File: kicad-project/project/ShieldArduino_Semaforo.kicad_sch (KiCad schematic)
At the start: 48 parts, among them IC1 TPS54302DDCR, J1 Conn_01x01, J10 Conn_01x01, J11 Conn_01x01, J12 Conn_01x01, J2 Conn_01x01, J3 Conn_01x01, J4 Conn_01x01, J5 Conn_01x01, J6 Conn_01x01, J7 Conn_01x01, J8 Conn_01x01, J9 Conn_01x01, P1 Power, P2 Analog, P3 Digital, P4 Digital, P5 CONN_01X01, P6 CONN_01X01, P7 CONN_01X01, P8 CONN_01X01, Q1 PMOS, U2 LM321, U4 MCP2542FD-E/MF

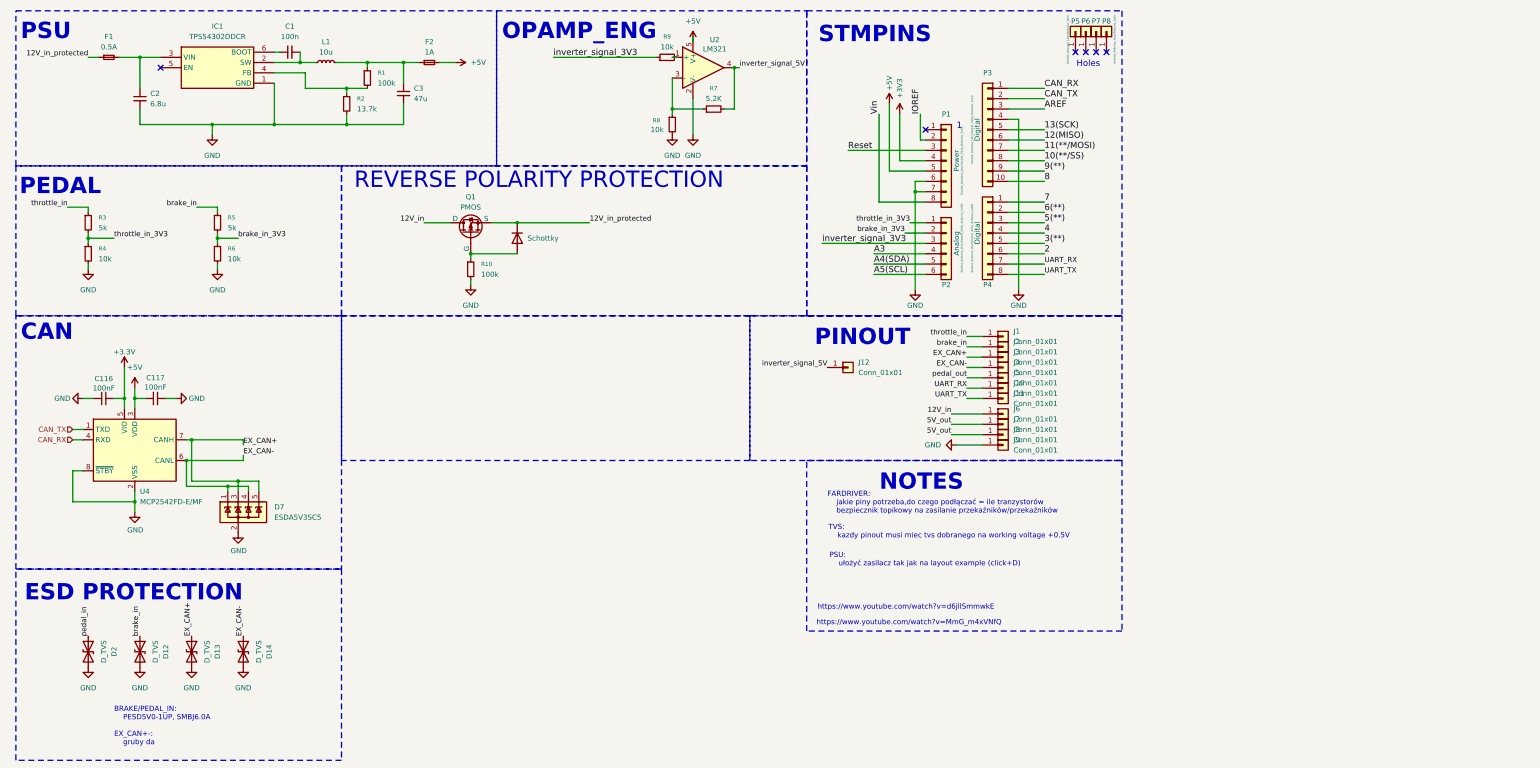
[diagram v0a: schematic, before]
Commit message: kicad-tvs_psu_pinout-update
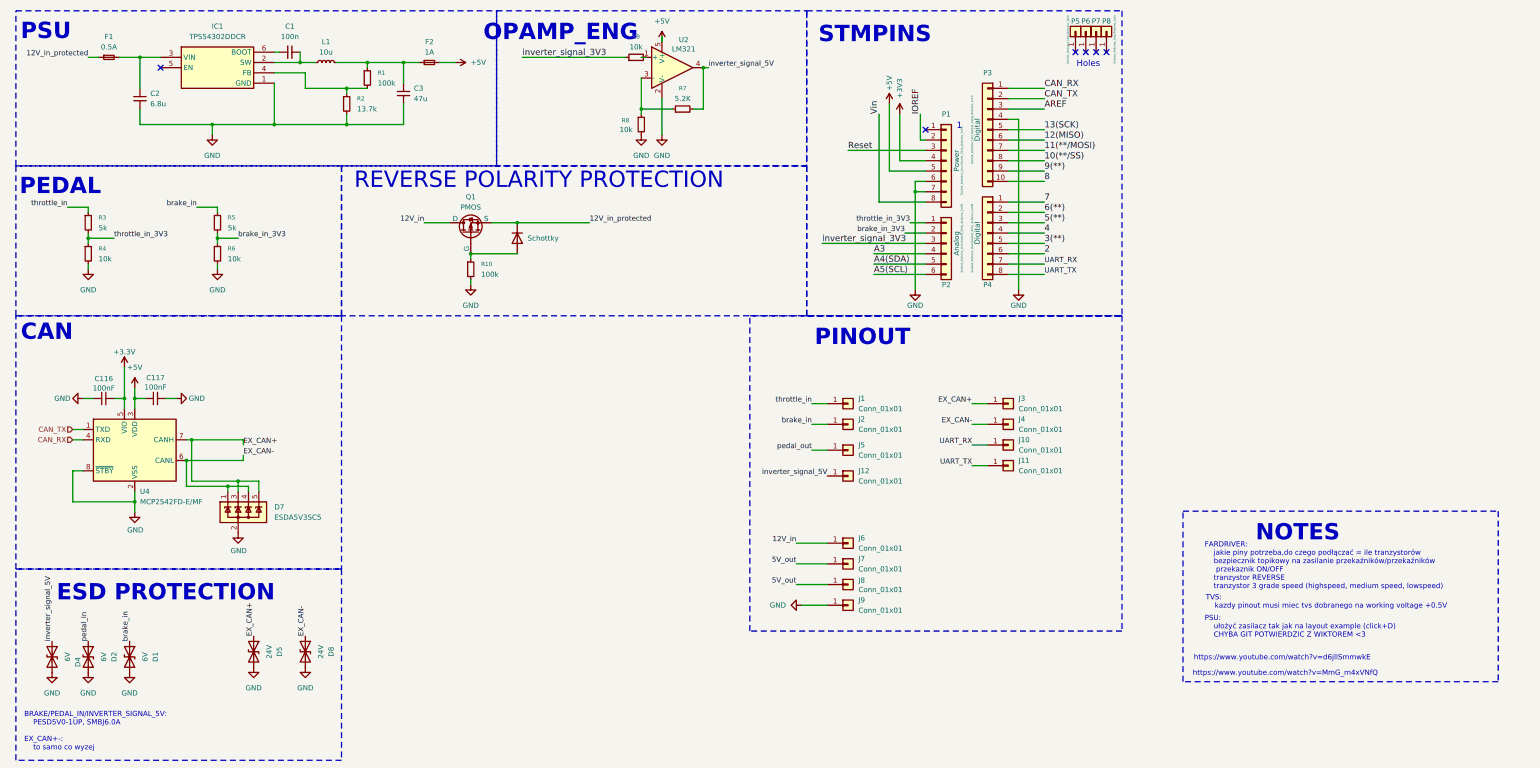
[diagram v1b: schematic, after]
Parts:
- removed D12, D13, D14: D_TVS, symbol Device:D_TVS
- added D1, D4: 6V, Diode_SMD:D_SMB_Handsoldering, symbol Device:D_TVS
- added D5, D8: 24V, Package_TO_SOT_SMD:SOT-23-3, symbol Device:D_TVS
- D2: value D_TVS -> 6V; footprint (none) -> Diode_SMD:D_SMB_Handsoldering
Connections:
- net EX_CAN+: now also D5.1 (A1)
- net EX_CAN-: now also D8.1 (A1)
- net GND: now also D1.2 (A2), D4.2 (A2), D5.2 (A2), D8.2 (A2)
- net brake_in: now also D1.1 (A1)
- net inverter_signal_5V: now also D4.1 (A1)
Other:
- note added: "BRAKE/PEDAL_IN/INVERTER_SIGNAL_5V: PESD5V0-1UP, SMBJ6.0A EX_CAN+-: to samo co wyzej"
- note added: "FARDRIVER: jakie piny potrzeba,do czego podłączać = ile tranzystorów bezpiecznik topikowy na zasilanie przekaźników/przekaźników przekaznik ON/OFF tranzystor REVERSE tranzystor 3 grade speed (highspeed, medium speed, lowspeed)"
- note added: "PSU: ułożyć zasilacz tak jak na layout example (click+D) CHYBA GIT POTWIERDZIC Z WIKTOREM <3"
- note removed: "BRAKE/PEDAL_IN: PESD5V0-1UP, SMBJ6.0A EX_CAN+-: gruby da"
- note removed: "FARDRIVER: jakie piny potrzeba,do czego podłączać = ile tranzystorów bezpiecznik topikowy na zasilanie przekaźników/przekaźników"
- note removed: "PSU: ułożyć zasilacz tak jak na layout example (click+D)"
- moved on the sheet: D2, J1, J10, J11, J12, J2, J3, J4, J5, J6, J7, J8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

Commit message: pcb-tests
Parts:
- removed C1: 100n, Capacitor_SMD:C_0805_2012Metric_Pad1.18x1.45mm_HandSolder, symbol Device:C_Small
- removed C2: 6.8u, Capacitor_SMD:C_0805_2012Metric_Pad1.18x1.45mm_HandSolder, symbol Device:C_Small
- removed C3: 47u, Capacitor_SMD:C_1210_3225Metric_Pad1.33x2.70mm_HandSolder, symbol Device:C_Small
- removed F2: 1A, Fuse:Fuse_2920_7451Metric_Pad2.10x5.45mm_HandSolder, symbol Device:Fuse_Small
- removed IC1: TPS54302DDCR, SOT95P280X110-6N, symbol TPS54302DDCR:TPS54302DDCR
- removed J11: Conn_01x01, Connector_Wire:SolderWire-0.1sqmm_1x01_D0.4mm_OD1mm_Relief, symbol Connector_Generic:Conn_01x01
- removed L1: 10u, Inductor_SMD:L_Bourns-SRN8040_8x8.15mm, symbol Device:L_Small
- removed R1: 100k, Resistor_SMD:R_0603_1608Metric_Pad0.98x0.95mm_HandSolder, symbol Device:R_Small
- removed R2: 13.7k, Resistor_SMD:R_0603_1608Metric_Pad0.98x0.95mm_HandSolder, symbol Device:R_Small
- added C119: 10u, Capacitor_SMD:C_0805_2012Metric_Pad1.18x1.45mm_HandSolder, symbol Device:C_Small
- added C120: 10uf, Capacitor_SMD:C_0805_2012Metric_Pad1.18x1.45mm_HandSolder, symbol Device:C_Small
- added C121: 100n 280mOhm, Capacitor_SMD:C_0805_2012Metric_Pad1.18x1.45mm_HandSolder, symbol Device:C_Small
- added C122, C123: 22u, Capacitor_SMD:C_0603_1608Metric_Pad1.08x0.95mm_HandSolder, symbol Device:C_Small
- added C134, C135, C136: 1uF, Capacitor_SMD:C_0603_1608Metric_Pad1.08x0.95mm_HandSolder, symbol Device:C_Small
- added C4, C5: 3.9uF, Capacitor_SMD:C_1206_3216Metric_Pad1.33x1.80mm_HandSolder, symbol Device:C_Small
- added D16: Diode TVS 12V, Diode_SMD:D_SOD-323F, symbol Device:D_TVS
- added D6: Schottky, Diode_SMD:D_SOD-123, symbol Device:D
- added F3: 3A, Fuse:Fuse_0603_1608Metric_Pad1.05x0.95mm_HandSolder, symbol Device:Fuse_Small
- added F3: 1A, Fuse:Fuse_0603_1608Metric_Pad1.05x0.95mm_HandSolder, symbol Device:Fuse_Small
- added IC2: TPS563200DDCR, footrpint:TPS563200DDCR, symbol TPS563200DDCR:TPS563200DDCR
- added J13, J14, J15, J16: Conn_01x01, Connector_Wire:SolderWire-0.1sqmm_1x01_D0.4mm_OD1mm_Relief, symbol Connector_Generic:Conn_01x01
- added K1: RELAY, footprint:PR412V4501A, symbol Relay:Fujitsu_FTR-LYAA005x
- added L2: 3.3u 20mOhm, footrpint:CLF7045__, symbol Device:L_Small
- added Q2, Q3, Q4, Q5: NMOS, Package_TO_SOT_SMD:SOT-23-3, symbol Simulation_SPICE:NMOS
- added R11, R12: 200, Resistor_SMD:R_0603_1608Metric_Pad0.98x0.95mm_HandSolder, symbol Device:R_Small
- added R13, R15, R17, R19: 100, Resistor_SMD:R_0805_2012Metric_Pad1.20x1.40mm_HandSolder, symbol Device:R_Small
- added R14, R16, R18, R20: 10k, Resistor_SMD:R_0805_2012Metric_Pad1.20x1.40mm_HandSolder, symbol Device:R_Small
- added R165: 56.2k 50mW, Resistor_SMD:R_0603_1608Metric_Pad0.98x0.95mm_HandSolder, symbol Device:R_Small
- added R166: 10k 50mW, Resistor_SMD:R_0603_1608Metric_Pad0.98x0.95mm_HandSolder, symbol Device:R_Small
- added TP12, TP14: TestPoint_Small, TestPoint:TestPoint_Pad_D1.0mm, symbol Connector:TestPoint_Small
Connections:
- net 5V_out is gone; now on net +5V: J7.1 (Pin_1), J8.1 (Pin_1)
- net +5V: now also F3.2, TP14.1
- net 12V_in_protected: now also F1.2, C134.1, C135.1, D16.2 (A2), D6.1 (K), F3.1, K1.1; no longer D3.1 (K), F1.1, Q1.3 (S)
- net GND: now also C119.2, C120.2, C122.2, C123.2, C134.2, C135.2, C136.2, C4.2, C5.2, D16.1 (A1), IC2.1 (GND), Q2.3 (S), Q3.3 (S), Q4.3 (S), Q5.3 (S), R14.2, R16.2, R166.1, R18.2, R20.2
- net UART_RX: no longer J10.1 (Pin_1)
- net brake_in_3V3: now also C5.1, R12.1; no longer R5.2, R6.1
- net throttle_in_3V3: now also C4.1, R11.1; no longer R3.2, R4.1
- net 2 renamed signal_high_speed
- net signal_high_speed: now also R17.1
- net 3(**) renamed signal_low_speed
- net signal_low_speed: now also R19.1
- net 4 renamed signal_reverse
- net signal_reverse: now also R15.1
- net 5(**) renamed signal_relay
- net signal_relay: now also R13.1
- new net: Q4.2 (G), R17.2, R18.1
- new net: R11.2, R3.2, R4.1
- new net: IC2.4 (VFB), R165.1, R166.2
- new net: C121.1, IC2.2 (SW), L2.1
- new net: C121.2, IC2.6 (VBST)
- new net: Q2.2 (G), R13.2, R14.1
- new net: Q3.2 (G), R15.2, R16.1
- new net: D6.2 (A), K1.4, Q2.1 (D)
- new net: D3.1 (K), F1.1, Q1.3 (S)
- new net: R12.2, R5.2, R6.1
- new net: Q5.2 (G), R19.2, R20.1
- new net  relay_in: J13.1 (Pin_1), K1.3
- new net +12V: C119.1, C120.1, F3.2, IC2.3 (VIN), IC2.5 (EN), TP12.1
- new net 5V_unfused: C122.1, C123.1, C136.1, F3.1, L2.2, R165.2
- new net high_speed: J10.1 (Pin_1), Q4.1 (D)
- new net low_speed: J16.1 (Pin_1), Q5.1 (D)
- new net relay_out: J14.1 (Pin_1), K1.2
- new net reverse: J15.1 (Pin_1), Q3.1 (D)
- no-connect marks 6 -> 5
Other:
- note added: "GPIO OUTPUT"
- note removed: "PSU"
- moved on the sheet: F1, R3, R4, R5, R6

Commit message: xd
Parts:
- removed F3: 1A, Fuse:Fuse_0603_1608Metric_Pad1.05x0.95mm_HandSolder, symbol Device:Fuse_Small
- removed L2: 3.3u 20mOhm, footrpint:CLF7045__, symbol Device:L_Small
- removed TP14: TestPoint_Small, TestPoint:TestPoint_Pad_D1.0mm, symbol Connector:TestPoint_Small
- added F4: 1A, Fuse:Fuse_0603_1608Metric_Pad1.05x0.95mm_HandSolder, symbol Device:Fuse_Small
- added L1: 3.3u 20mOhm, footprint:CLF7045__, symbol Device:L_Small
- IC2: footprint footrpint:TPS563200DDCR -> footprint:TPS563200DDCR
- renumbered C116 to C1, C4 to C2, C117 to C4, C5 to C7, D4 to D1, D1 to D4, D7 to D5, D5 to D6, D8 to D7, D6 to D8, D3 to D9, F1 to F2, J4 to J10, J13 to J11, J14 to J12, J15 to J13, J16 to J14, J10 to J15, J5 to J3, J12 to J4, J6 to J5, J7 to J6, J8 to J7, J9 to J8, J3 to J9, Q4 to Q3, Q3 to Q4, R3 to R1, R18 to R10, R10 to R11, R9 to R14, R8 to R16, R16 to R17, R19 to R18, R7 to R19, R4 to R2, R11 to R3, R5 to R4, R6 to R5, R12 to R6, R13 to R7, R17 to R8, R14 to R9, U4 to U1
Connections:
- net +5V: now also F4.2
- net 5V_unfused: now also F4.1, L1.2
- net at C121.1, IC2.2 (SW): now also L1.1
- net +12V: no longer names the net of C119.1, C120.1, F3.2, IC2.3 (VIN), IC2.5 (EN), TP12.1
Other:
- moved on the sheet: C119, C120, C121, C122, C123, C134, C135, C136, D16, IC2, R165, R166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

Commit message: kicad-schematic_cleanup
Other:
- note added: "HIGH SPEED"
- note added: "LOW SPEED"
- note added: "POWER SUPPLY UNIT"
- note added: "RELAY CONTROL"
- note added: "REVERSE GEAR"
- note added: "REVERSE POLARITY CONTROL"
- note removed: "REVERSE POLARITY PROTECTION"
- moved on the sheet: C1, C119, C120, C121, C122, C123, C134, C135, C136, C2, C4, C7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

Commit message: kicad-work
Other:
- note added: "INNY FOOTPRINT NIZ TEN SCHEMAT PRZEKAZNIKA 4,2 w innych miejscach"
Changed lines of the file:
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@@
 		)
 	)
+	(text "INNY FOOTPRINT NIZ TEN SCHEMAT PRZEKAZNIKA 4,2 w innych miejscach\n"
+		(exclude_from_sim no)
+		(at 59.182 166.878 0)
+		(effects
+			(font
+				(size 1.27 1.27)
+			)
+		)
+	)
 	(text "STMPINS"
 		(exclude_from_sim no)
@@
 		)
 	)
+	(label "CAN_RX"
+		(at 340.36 120.65 180)
+		(effects
+			(font
+				(size 1.524 1.524)
+			)
+			(justify right bottom)
+		)
+	)
 	(label "signal_reverse"
 		(at 120.65 170.18 180)
@@
 		)
 	)
+	(label "CAN_TX"
+		(at 340.36 118.11 180)
+		(effects
+			(font
+				(size 1.524 1.524)
+			)
+			(justify right bottom)
+		)
+	)
 	(label "UART_RX"
 		(at 226.06 74.93 0)
@@
 		)
 	)
-	(hierarchical_label "CAN_RX"
-		(shape input)
-		(at 340.36 120.65 180)
-		(effects
-			(font
-				(size 1.27 1.27)
-			)
-			(justify right)
-		)
-	)
 	(hierarchical_label "0V_OUT"
 		(shape input)
@@
 		)
 	)
-	(hierarchical_label "CAN_TX"
-		(shape input)
-		(at 340.36 118.11 180)
-		(effects
-			(font
-				(size 1.27 1.27)
-			)
-			(justify right)
-		)
-	)

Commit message: kicad-pcb
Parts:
- removed J1, J10, J11, J12, J13, J14, J15, J2, J3, J4, J5, J6, J7, J8, J9: Conn_01x01, Connector_Wire:SolderWire-0.1sqmm_1x01_D0.4mm_OD1mm_Relief, symbol Connector_Generic:Conn_01x01
- added J1: Conn_01x15, footprint:L17HTHES4R1C, symbol Connector_Generic:Conn_01x15
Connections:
- net  relay_in: now also J1.1 (Pin_1)
- net +5V: now also J1.13 (Pin_13), J1.14 (Pin_14)
- net 12V_in: now also J1.12 (Pin_12)
- net EX_CAN+: now also J1.10 (Pin_10)
- net EX_CAN-: now also J1.11 (Pin_11)
- net GND: now also J1.15 (Pin_15)
- net brake_in: now also J1.7 (Pin_7)
- net high_speed: now also J1.5 (Pin_5)
- net inverter_signal_5V: now also J1.9 (Pin_9)
- net low_speed: now also J1.4 (Pin_4)
- net pedal_out: now also J1.8 (Pin_8)
- net relay_out: now also J1.2 (Pin_2)
- net reverse: now also J1.3 (Pin_3)
- net throttle_in: now also J1.6 (Pin_6)

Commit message: kicad-project-layout-v0.5
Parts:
- removed TP12: TestPoint_Small, TestPoint:TestPoint_Pad_D1.0mm, symbol Connector:TestPoint_Small
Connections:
- net 12V_in: now also J1.15 (Pin_15); no longer J1.12 (Pin_12)
- net EX_CAN+: now also D5.4 (K); no longer D5.5 (K)
- net EX_CAN-: now also D5.5 (K); no longer D5.4 (K)
- net GND: now also J1.12 (Pin_12); no longer J1.15 (Pin_15)
